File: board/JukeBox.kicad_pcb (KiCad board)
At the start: 2 copper layers, 78.5 x 78.5 mm, 39 parts, among them J1 USB_C_Receptacle_USB2.0, SW1 SW_SPST, SW10 SW_SPST, SW11 SW_SPST, SW12 SW_SPST, SW2 SW_SPST, SW3 SW_SPST, SW4 SW_SPST, SW5 SW_SPST, SW6 SW_SPST, SW7 SW_SPST, SW8 SW_SPST, SW9 SW_SPST, U1 ATmega8U2-A, Y1 16MHz

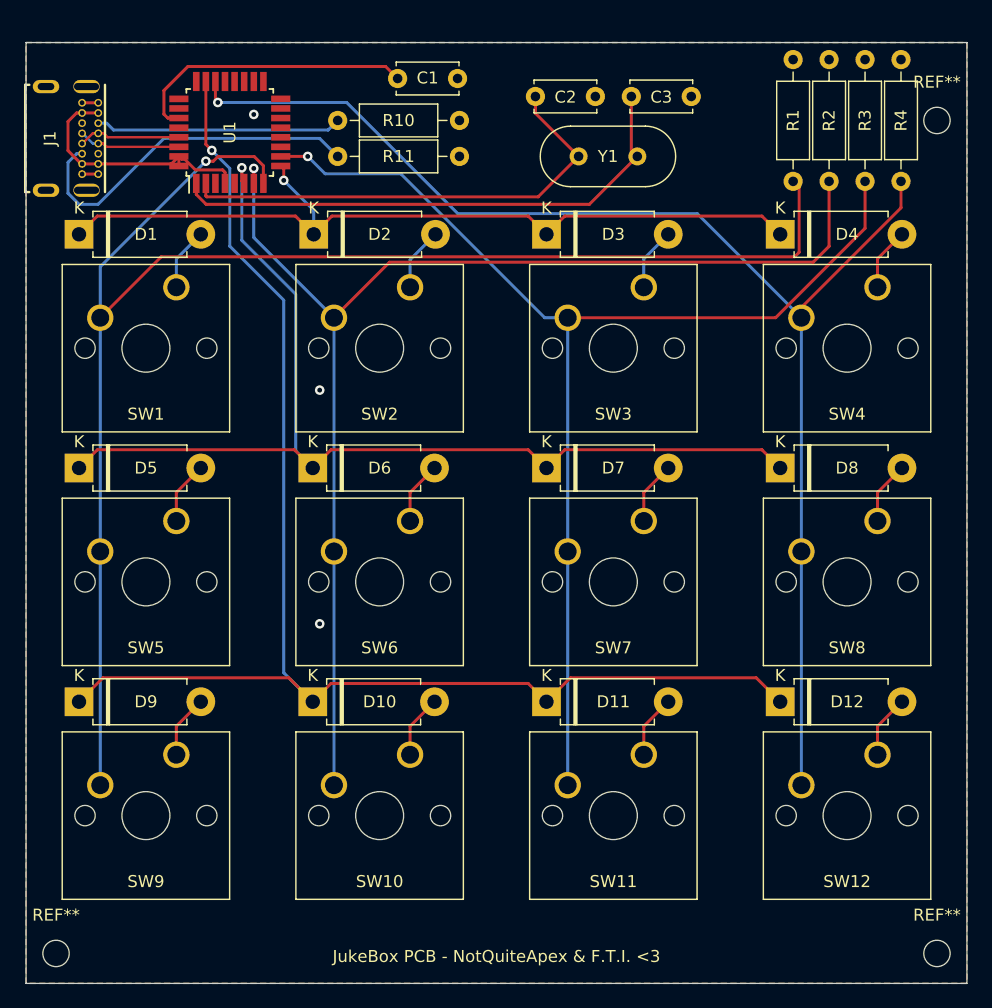
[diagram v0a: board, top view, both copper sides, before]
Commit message: update naming, add headers for direct connection
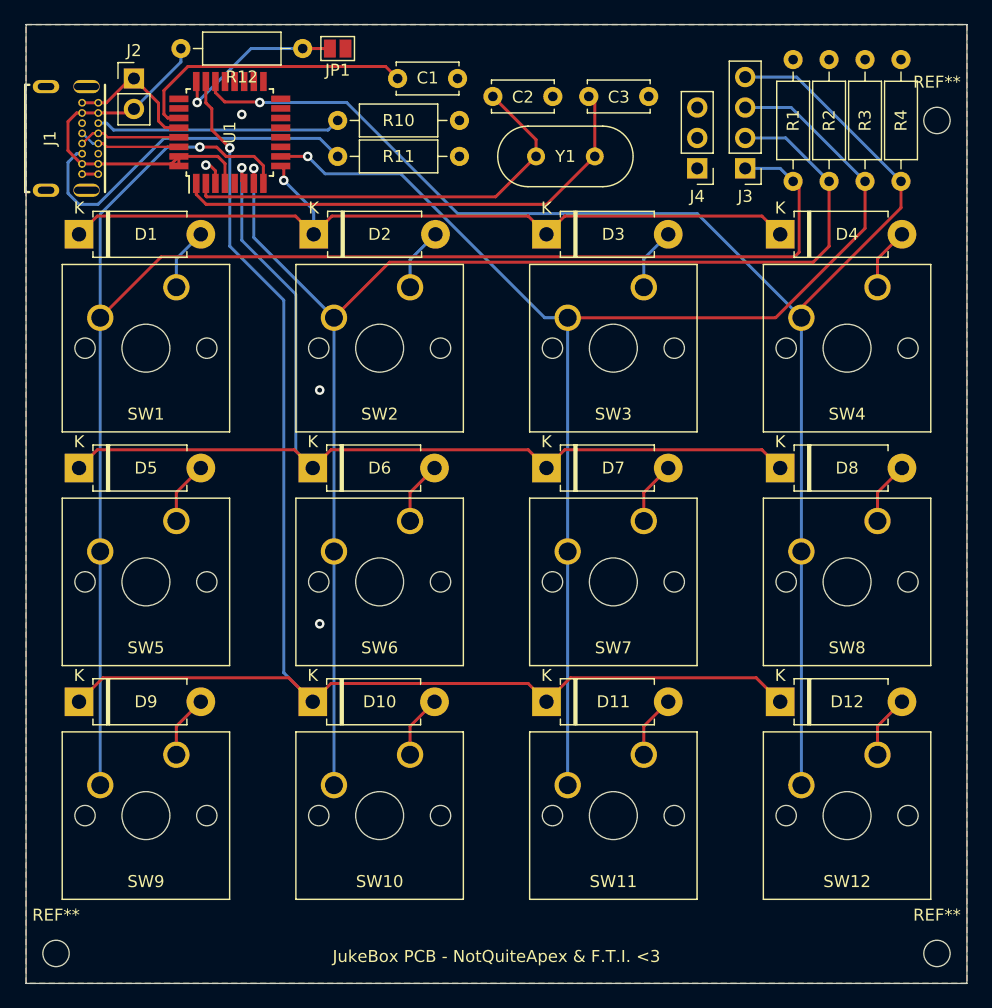
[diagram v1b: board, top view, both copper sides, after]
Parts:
- added J2: Conn_01x02, Connector_PinHeader_2.54mm:PinHeader_1x02_P2.54mm_Vertical, F.Cu at (116.0, 39.5)
- added J3: Conn_01x04, Connector_PinHeader_2.54mm:PinHeader_1x04_P2.54mm_Vertical, F.Cu at (167.0, 47.0)
- added J4: Conn_01x03, Connector_PinHeader_2.54mm:PinHeader_1x03_P2.54mm_Vertical, F.Cu at (163.0, 47.0)
- added JP1: , Jumper:SolderJumper-2_P1.3mm_Open_Pad1.0x1.5mm, F.Cu at (133.0, 37.0)
- added R12: 10K, Resistor_THT:R_Axial_DIN0207_L6.3mm_D2.5mm_P10.16mm_Horizontal, F.Cu at (130.1, 37.0)
- moved C2 3.55 mm to (150.9, 41.0)
- moved C3 3.55 mm to (158.9, 41.0)
- moved Y1 3.55 mm to (154.4, 46.0)
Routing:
- net COL_4: track 111.8 -> 128.0 mm
- net Net-(JP1-Pad2): track 0.00 -> 14.7 mm, vias 0 -> 1
- net COL_3: track 100.3 -> 112.9 mm
- net GND: track 2.70 -> 15.0 mm, vias 3 -> 4
- net +5V: track 21.3 -> 31.0 mm
- net COL_2: track 104.7 -> 113.2 mm
- net COL_1: track 129.2 -> 136.8 mm
- net Net-(C3-Pad2): track 44.9 -> 41.4 mm
- net Net-(C2-Pad2): track 40.1 -> 36.5 mm
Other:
- board size 78.5 x 78.5 mm -> 78.5 x 80 mm

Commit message: route headers for direct access to keys
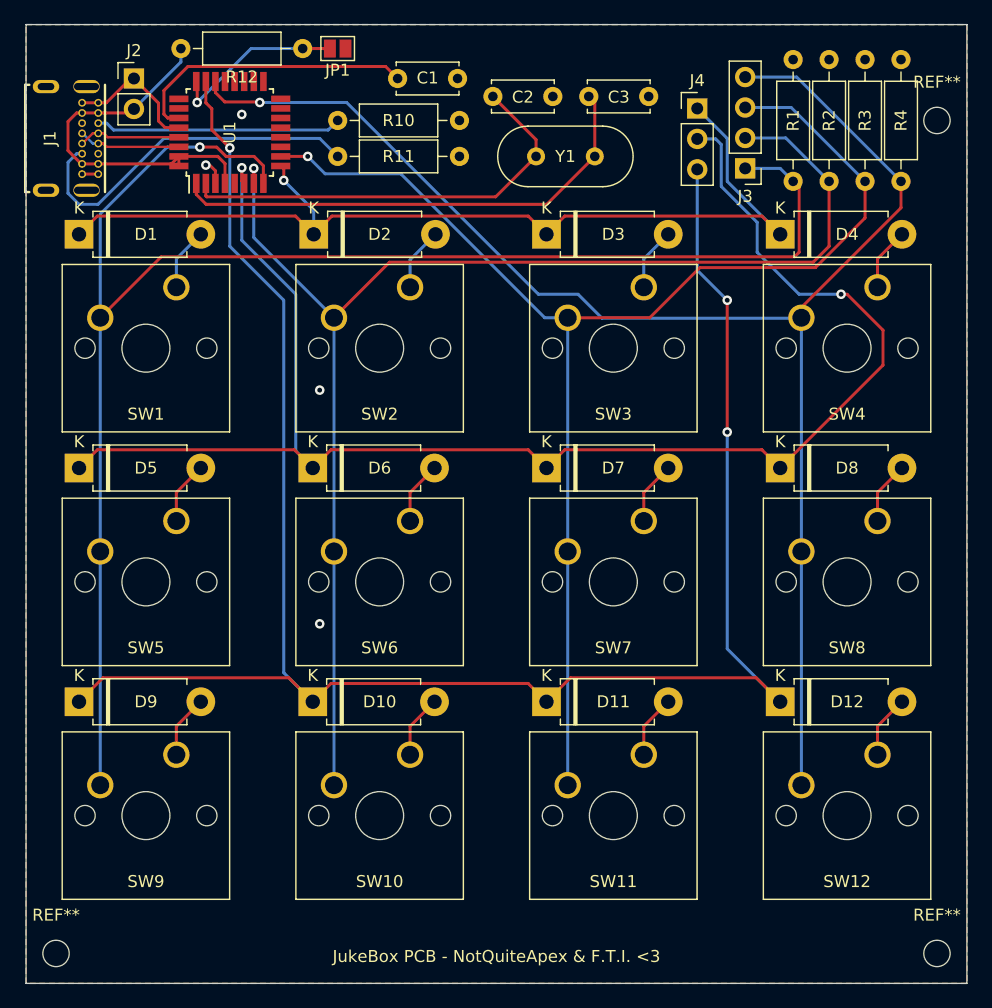
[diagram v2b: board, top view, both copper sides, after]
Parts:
- moved J4 5.00 mm to (163.0, 42.0), turned to 0 degrees
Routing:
- net ROW_3: track 118.5 -> 165.8 mm, vias 1 -> 3
- net ROW_2: track 91.2 -> 131.9 mm, vias 1 -> 2
- net ROW_1: track 69.1 -> 82.5 mm
- net COL_3: track 112.9 -> 112.4 mm
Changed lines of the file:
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@@
   )
   (footprint "Connector_PinHeader_2.54mm:PinHeader_1x03_P2.54mm_Vertical" (layer "F.Cu")
-    (at 163 47 180)
+    (at 163 42)
     (descr "Through hole straight pin header, 1x03, 2.54mm pitch, single row")
     (tags "Through hole pin header THT 1x03 2.54mm single row")
@@
     (fp_line (start -1.27 6.35) (end -1.27 -0.635) (layer "F.Fab") (width 0.1))
     (fp_line (start -1.27 -0.635) (end -0.635 -1.27) (layer "F.Fab") (width 0.1))
-    (pad "1" thru_hole rect (at 0 0 180) (size 1.7 1.7) (drill 1) (layers *.Cu *.Mask)
+    (pad "1" thru_hole rect (at 0 0) (size 1.7 1.7) (drill 1) (layers *.Cu *.Mask)
       (net 5 "ROW_1") (pinfunction "Pin_1") (pintype "passive"))
-    (pad "2" thru_hole oval (at 0 2.54 180) (size 1.7 1.7) (drill 1) (layers *.Cu *.Mask)
+    (pad "2" thru_hole oval (at 0 2.54) (size 1.7 1.7) (drill 1) (layers *.Cu *.Mask)
       (net 10 "ROW_2") (pinfunction "Pin_2") (pintype "passive"))
-    (pad "3" thru_hole oval (at 0 5.08 180) (size 1.7 1.7) (drill 1) (layers *.Cu *.Mask)
+    (pad "3" thru_hole oval (at 0 5.08) (size 1.7 1.7) (drill 1) (layers *.Cu *.Mask)
       (net 15 "ROW_3") (pinfunction "Pin_3") (pintype "passive"))
     (model "${KICAD6_3DMODEL_DIR}/Connector_PinHeader_2.54mm.3dshapes/PinHeader_1x03_P2.54mm_Vertical.wrl"
@@
   (segment (start 132.525 50.975) (end 131 52.5) (width 0.25) (layer "F.Cu") (net 5))
   (via (at 128.5 48) (size 0.8) (drill 0.4) (layers "F.Cu" "B.Cu") (net 5))
+  (segment (start 165.5 48.08) (end 165.5 44.5) (width 0.25) (layer "B.Cu") (net 5))
+  (segment (start 165.5 44.5) (end 163 42) (width 0.25) (layer "B.Cu") (net 5))
+  (segment (start 169.92 52.5) (end 165.5 48.08) (width 0.25) (layer "B.Cu") (net 5))
   (segment (start 131 50.5) (end 128.5 48) (width 0.25) (layer "B.Cu") (net 5))
   (segment (start 131 52.5) (end 131 50.5) (width 0.25) (layer "B.Cu") (net 5))
@@
   (segment (start 178.04 54.54) (end 180.08 52.5) (width 0.25) (layer "F.Cu") (net 9))
   (segment (start 178.04 56.92) (end 178.04 54.54) (width 0.25) (layer "F.Cu") (net 9))
+  (segment (start 175.5 57.5) (end 178.5 60.5) (width 0.25) (layer "F.Cu") (net 10))
   (segment (start 129.395 70.475) (end 112.945 70.475) (width 0.25) (layer "F.Cu") (net 10))
+  (segment (start 175 57.5) (end 175.5 57.5) (width 0.25) (layer "F.Cu") (net 10))
   (segment (start 132.445 70.475) (end 130.92 72) (width 0.25) (layer "F.Cu") (net 10))
+  (segment (start 178.5 63.42) (end 169.92 72) (width 0.25) (layer "F.Cu") (net 10))
   (segment (start 150.42 72) (end 148.895 70.475) (width 0.25) (layer "F.Cu") (net 10))
   (segment (start 112.945 70.475) (end 111.42 72) (width 0.25) (layer "F.Cu") (net 10))
@@
   (segment (start 151.945 70.475) (end 150.42 72) (width 0.25) (layer "F.Cu") (net 10))
   (segment (start 168.395 70.475) (end 151.945 70.475) (width 0.25) (layer "F.Cu") (net 10))
+  (segment (start 178.5 60.5) (end 178.5 63.42) (width 0.25) (layer "F.Cu") (net 10))
   (segment (start 148.895 70.475) (end 132.445 70.475) (width 0.25) (layer "F.Cu") (net 10))
   (segment (start 130.92 72) (end 129.395 70.475) (width 0.25) (layer "F.Cu") (net 10))
   (via (at 125.001881 46.947456) (size 0.8) (drill 0.4) (layers "F.Cu" "B.Cu") (net 10))
+  (via (at 175 57.5) (size 0.8) (drill 0.4) (layers "F.Cu" "B.Cu") (net 10))
   (segment (start 129.5 57.5) (end 125.001881 53.001881) (width 0.25) (layer "B.Cu") (net 10))
+  (segment (start 165 48.5) (end 168 51.5) (width 0.25) (layer "B.Cu") (net 10))
+  (segment (start 163 44.54) (end 164.54 44.54) (width 0.25) (layer "B.Cu") (net 10))
+  (segment (start 168 54) (end 171.5 57.5) (width 0.25) (layer "B.Cu") (net 10))
   (segment (start 125.001881 53.001881) (end 125.001881 46.947456) (width 0.25) (layer "B.Cu") (net 10))
   (segment (start 129.5 70.58) (end 129.5 57.5) (width 0.25) (layer "B.Cu") (net 10))
+  (segment (start 165 45) (end 165 48.5) (width 0.25) (layer "B.Cu") (net 10))
+  (segment (start 168 51.5) (end 168 54) (width 0.25) (layer "B.Cu") (net 10))
+  (segment (start 164.54 44.54) (end 165 45) (width 0.25) (layer "B.Cu") (net 10))
+  (segment (start 171.5 57.5) (end 175 57.5) (width 0.25) (layer "B.Cu") (net 10))
   (segment (start 130.92 72) (end 129.5 70.58) (width 0.25) (layer "B.Cu") (net 10))
   (segment (start 119.54 74.04) (end 121.58 72) (width 0.25) (layer "F.Cu") (net 11))
@@
   (segment (start 150.42 91.5) (end 152.42 89.5) (width 0.25) (layer "F.Cu") (net 15))
   (segment (start 130.92 91.5) (end 132.445 89.975) (width 0.25) (layer "F.Cu") (net 15))
+  (segment (start 165.5 58) (end 165.5 69) (width 0.25) (layer "F.Cu") (net 15))
   (segment (start 122 41.525305) (end 122 39.75) (width 0.25) (layer "F.Cu") (net 15))
   (segment (start 111.42 91.5) (end 113.42 89.5) (width 0.25) (layer "F.Cu") (net 15))
@@
   (segment (start 132.445 89.975) (end 148.895 89.975) (width 0.25) (layer "F.Cu") (net 15))
   (via (at 124 45.288153) (size 0.8) (drill 0.4) (layers "F.Cu" "B.Cu") (net 15))
+  (via (at 165.5 58) (size 0.8) (drill 0.4) (layers "F.Cu" "B.Cu") (net 15))
+  (via (at 165.5 69) (size 0.8) (drill 0.4) (layers "F.Cu" "B.Cu") (net 15))
   (segment (start 128.5 58) (end 128.5 89.08) (width 0.25) (layer "B.Cu") (net 15))
   (segment (start 124 53.5) (end 128.5 58) (width 0.25) (layer "B.Cu") (net 15))
+  (segment (start 163 47.08) (end 163 55.5) (width 0.25) (layer "B.Cu") (net 15))
   (segment (start 124 45.288153) (end 124 53.5) (width 0.25) (layer "B.Cu") (net 15))
+  (segment (start 165.5 87.08) (end 169.92 91.5) (width 0.25) (layer "B.Cu") (net 15))
+  (segment (start 163 55.5) (end 165.5 58) (width 0.25) (layer "B.Cu") (net 15))
+  (segment (start 165.5 69) (end 165.5 87.08) (width 0.25) (layer "B.Cu") (net 15))
   (segment (start 128.5 89.08) (end 130.92 91.5) (width 0.25) (layer "B.Cu") (net 15))
   (segment (start 119.54 95.92) (end 119.54 93.54) (width 0.25) (layer "F.Cu") (net 16))
@@
   (segment (start 170.38 44.46) (end 174 48.08) (width 0.25) (layer "B.Cu") (net 29))
   (segment (start 132.69 78.96) (end 132.69 98.46) (width 0.25) (layer "B.Cu") (net 29))
-  (segment (start 169.54 59.46) (end 152.19 59.46) (width 0.25) (layer "F.Cu") (net 30))
+  (segment (start 159.04 59.46) (end 152.19 59.46) (width 0.25) (layer "F.Cu") (net 30))
+  (segment (start 172.859946 55.27645) (end 163.22355 55.27645) (width 0.25) (layer "F.Cu") (net 30))
+  (segment (start 177 51.136396) (end 172.859946 55.27645) (width 0.25) (layer "F.Cu") (net 30))
   (segment (start 130.5 46) (end 128.25 46) (width 0.25) (layer "F.Cu") (net 30))
-  (segment (start 177 48.08) (end 177 52) (width 0.25) (layer "F.Cu") (net 30))
-  (segment (start 177 52) (end 169.54 59.46) (width 0.25) (layer "F.Cu") (net 30))
+  (segment (start 177 48.08) (end 177 51.136396) (width 0.25) (layer "F.Cu") (net 30))
+  (segment (start 163.22355 55.27645) (end 159.04 59.46) (width 0.25) (layer "F.Cu") (net 30))
   (via (at 130.5 46) (size 0.8) (drill 0.4) (layers "F.Cu" "B.Cu") (net 30))
   (segment (start 152.19 98.46) (end 152.19 78.96) (width 0.25) (layer "B.Cu") (net 30))
@@
   (segment (start 126.5 41.5) (end 126.456895 41.456895) (width 0.25) (layer "F.Cu") (net 31))
   (via (at 126.5 41.5) (size 0.8) (drill 0.4) (layers "F.Cu" "B.Cu") (net 31))
+  (segment (start 167 39.38) (end 171.3 39.38) (width 0.25) (layer "B.Cu") (net 31))
+  (segment (start 153.052373 57.5) (end 155.052373 59.5) (width 0.25) (layer "B.Cu") (net 31))
+  (segment (start 171.69 59.46) (end 171.69 78.96) (width 0.25) (layer "B.Cu") (net 31))
+  (segment (start 155.052373 59.5) (end 171.65 59.5) (width 0.25) (layer "B.Cu") (net 31))
+  (segment (start 171.69 78.96) (end 171.69 98.46) (width 0.25) (layer "B.Cu") (net 31))
+  (segment (start 171.65 59.5) (end 171.69 59.46) (width 0.25) (layer "B.Cu") (net 31))
+  (segment (start 133.748602 41.5) (end 149.748602 57.5) (width 0.25) (layer "B.Cu") (net 31))
+  (segment (start 171.3 39.38) (end 180 48.08) (width 0.25) (layer "B.Cu") (net 31))
   (segment (start 126.5 41.5) (end 133.748602 41.5) (width 0.25) (layer "B.Cu") (net 31))
-  (segment (start 167 39.38) (end 171.3 39.38) (width 0.25) (layer "B.Cu") (net 31))
-  (segment (start 171.69 59.46) (end 171.69 78.96) (width 0.25) (layer "B.Cu") (net 31))
-  (segment (start 163 50.77) (end 171.69 59.46) (width 0.25) (layer "B.Cu") (net 31))
-  (segment (start 171.69 78.96) (end 171.69 98.46) (width 0.25) (layer "B.Cu") (net 31))
-  (segment (start 171.3 39.38) (end 180 48.08) (width 0.25) (layer "B.Cu") (net 31))
-  (segment (start 133.748602 41.5) (end 143.018602 50.77) (width 0.25) (layer "B.Cu") (net 31))
-  (segment (start 143.018602 50.77) (end 163 50.77) (width 0.25) (layer "B.Cu") (net 31))
+  (segment (start 149.748602 57.5) (end 153.052373 57.5) (width 0.25) (layer "B.Cu") (net 31))
   (zone (net 1) (net_name "GND") (layer "F.Cu") (hatch edge 0.508)
     (connect_pads (clearance 0.508))

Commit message: add kailh choc switches in place of cherry mx's
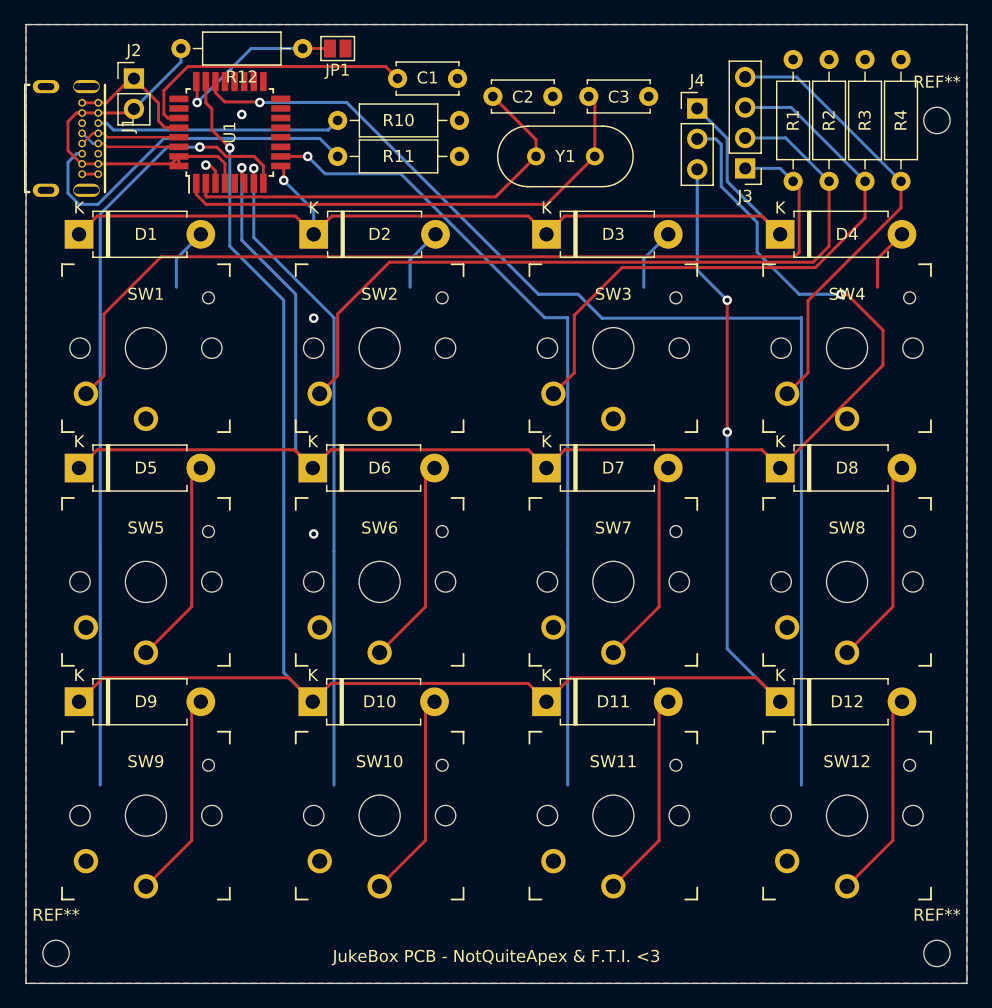
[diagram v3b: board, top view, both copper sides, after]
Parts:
- J1: footprint USB4085-GF-A:GCT_USB4085-GF-A_REVA4 -> jukebox-footprints:GCT_USB4085-GF-A_REVA4
- SW1, SW10, SW11, SW12, SW2, SW3, SW4, SW5, SW6, SW7, SW8, SW9: footprint Button_Switch_Keyboard:SW_Cherry_MX_1.00u_PCB -> jukebox-footprints:Kailh_PG1350
- moved SW1 5.68 mm to (117.0, 62.0)
- moved SW5 5.68 mm to (117.0, 81.5)
- moved SW9 5.68 mm to (117.0, 101.0)
- moved SW10 5.68 mm to (136.5, 101.0)
- moved SW11 5.68 mm to (156.0, 101.0)
- moved SW12 5.68 mm to (175.5, 101.0)
- moved SW2 5.68 mm to (136.5, 62.0)
- moved SW3 5.68 mm to (156.0, 62.0)
- moved SW4 5.68 mm to (175.5, 62.0)
- moved SW6 5.68 mm to (136.5, 81.5)
- moved SW7 5.68 mm to (156.0, 81.5)
- moved SW8 5.68 mm to (175.5, 81.5)
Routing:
- net Net-(D9-Pad2): track 5.26 -> 17.3 mm
- net Net-(D5-Pad2): track 5.26 -> 17.3 mm
- net Net-(D7-Pad2): track 5.26 -> 17.3 mm
- net Net-(D12-Pad2): track 5.26 -> 17.3 mm
- net Net-(D11-Pad2): track 5.26 -> 17.3 mm
- net Net-(D10-Pad2): track 5.26 -> 17.3 mm
- net Net-(D8-Pad2): track 5.26 -> 17.3 mm
- net Net-(D6-Pad2): track 5.26 -> 17.3 mm
- net COL_4: track 128.1 -> 134.9 mm
- net COL_1: track 136.8 -> 143.7 mm
- net COL_2: track 113.2 -> 120.0 mm
- net COL_3: track 112.4 -> 119.0 mm
